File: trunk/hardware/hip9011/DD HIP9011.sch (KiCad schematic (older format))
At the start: 25 parts, among them P1 KNOCK 1, P2 KNOCK 2, P3 12V, P4 CONN_4X2, U1 78L05, X1 4MHz

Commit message: v 2
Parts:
- removed U1: 78L05, TSOP89, symbol 78L05
- removed X1: 4MHz, ~, symbol QUARTZCMS4
- added R10, R11, R12, R13, R14: 1K, ~, symbol R
- added U1: 7805-SOT89, ~, symbol 7805-SOT89
- added X1: QUARTZ, ~, symbol QUARTZ
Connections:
- net labels added: +12V, +5V, CS, GND, INT/HLD, INTOUT, SCK, SI, SO, TEST
- wire segments 78 -> 67
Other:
- note added: "DD HIP9011 ver.2\nRusEfi.com"
- moved on the sheet: C1, C2, C3, C4, C5, C6, C7, C8, D1, D2, P1, P2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

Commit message: with logo
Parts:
- added G1: LOGO, symbol LOGO
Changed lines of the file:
@@
 LIBS:quartz
 LIBS:7805-sot89
+LIBS:logo_flipped
 LIBS:DD HIP9011-cache
 EELAYER 27 0
@@
 Text Notes 1600 1700 0    118  ~ 0
 DD HIP9011 ver.2\nRusEfi.com
+$Comp
+L LOGO G1
+U 1 1 52A2A9AB
+P 2800 5300
+F 0 "G1" H 2800 5197 60  0001 C CNN
+F 1 "LOGO" H 2800 5403 60  0001 C CNN
+F 2 "" H 2800 5300 60  0000 C CNN
+F 3 "" H 2800 5300 60  0000 C CNN
+	1    2800 5300
+	1    0    0    -1
+$EndComp
 $EndSCHEMATC

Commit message: newer version
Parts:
- added R15, R16: 10k, ~, symbol R
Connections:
- net labels added: OUT
- wire segments 67 -> 66
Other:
- note added: "DD HIP9011 ver 0.1\nRusEfi.com"
- note removed: "DD HIP9011 ver.2\nRusEfi.com"
- moved on the sheet: U1
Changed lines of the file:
@@
 Sheet 1 1
 Title "noname.sch"
-Date "7 dec 2013"
+Date "8 dec 2013"
 Rev ""
 Comp ""
@@
 Wire Wire Line
 	2050 4450 2050 4250
-Wire Wire Line
-	2650 4450 2650 4350
 Connection ~ 2200 4450
 Connection ~ 3300 4050
-Connection ~ 2650 4450
 Connection ~ 3300 4450
 Wire Wire Line
@@
 Text Label 7200 4750 0    60   ~ 0
 CS
-Text Label 8500 4750 0    60   ~ 0
-INTOUT
 Wire Wire Line
 	4650 4350 4350 4350
@@
 L 7805-SOT89 U1
 U 1 1 52A25C32
-P 2650 4100
-F 0 "U1" H 2800 3904 60  0000 C CNN
-F 1 "7805-SOT89" H 2650 4300 60  0000 C CNN
-F 2 "~" H 2650 4100 60  0000 C CNN
-F 3 "~" H 2650 4100 60  0000 C CNN
-	1    2650 4100
-	1    0    0    -1
+P 2650 4000
+F 0 "U1" H 2800 3804 60  0000 C CNN
+F 1 "7805-SOT89" H 2650 4200 60  0000 C CNN
+F 2 "~" H 2650 4000 60  0000 C CNN
+F 3 "~" H 2650 4000 60  0000 C CNN
+	1    2650 4000
+	-1   0    0    1
 $EndComp
 Text Label 2200 4050 0    60   ~ 0
 +12V
 Text Notes 1600 1700 0    118  ~ 0
-DD HIP9011 ver.2\nRusEfi.com
+DD HIP9011 ver 0.1\nRusEfi.com
+$Comp
+L R R15
+U 1 1 52A2E159
+P 8400 3450
+F 0 "R15" V 8480 3450 40  0000 C CNN
+F 1 "10k" V 8407 3451 40  0000 C CNN
+F 2 "~" V 8330 3450 30  0000 C CNN
+F 3 "~" H 8400 3450 30  0000 C CNN
+	1    8400 3450
+	1    0    0    -1
+$EndComp
+$Comp
+L R R16
+U 1 1 52A2E168
+P 8400 3950
+F 0 "R16" V 8480 3950 40  0000 C CNN
+F 1 "10k" V 8407 3951 40  0000 C CNN
+F 2 "~" V 8330 3950 30  0000 C CNN
+F 3 "~" H 8400 3950 30  0000 C CNN
+	1    8400 3950
+	1    0    0    -1
+$EndComp
+Text Label 8400 4200 0    60   ~ 0
+GND
+Text Label 8400 3700 0    60   ~ 0
+OUT
+Text Label 8400 3200 0    60   ~ 0
+INTOUT
+Text Label 8500 4750 0    60   ~ 0
+OUT
+Text Label 2650 3750 0    60   ~ 0
+GND
 $Comp
 L LOGO G1
-U 1 1 52A2A9AB
-P 2800 5300
-F 0 "G1" H 2800 5197 60  0001 C CNN
-F 1 "LOGO" H 2800 5403 60  0001 C CNN
-F 2 "" H 2800 5300 60  0000 C CNN
-F 3 "" H 2800 5300 60  0000 C CNN
-	1    2800 5300
-	1    0    0    -1
-$EndComp
+U 1 1 52A3E360
+P 3800 1700
+F 0 "G1" H 3800 1597 60  0001 C CNN
+F 1 "LOGO" H 3800 1803 60  0001 C CNN
+F 2 "" H 3800 1700 60  0000 C CNN
+F 3 "" H 3800 1700 60  0000 C CNN
+	1    3800 1700
+	1    0    0    -1
+$EndComp

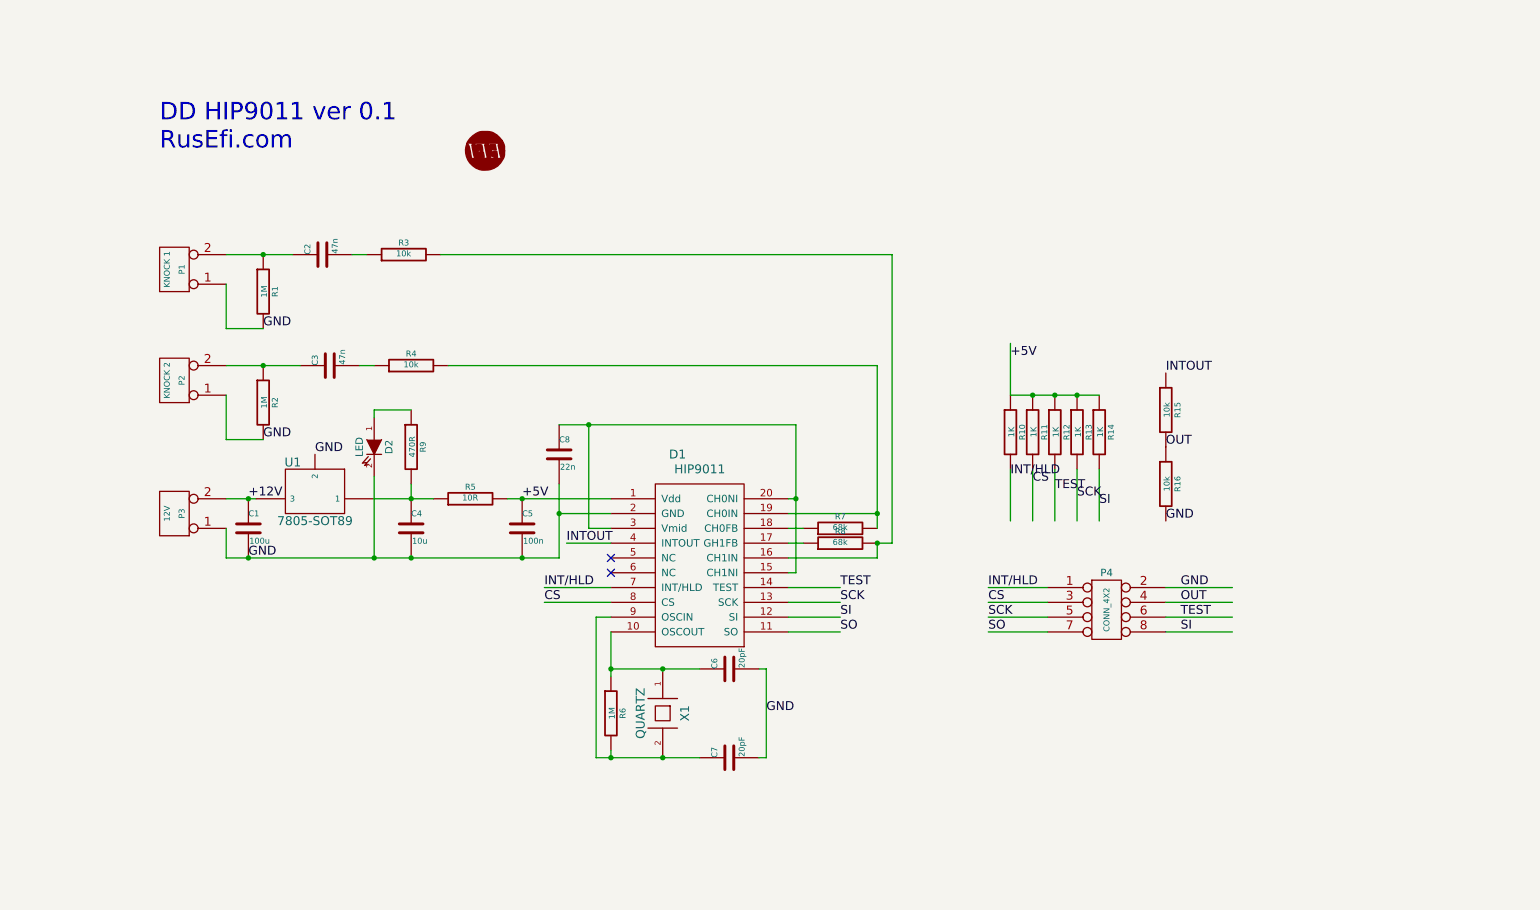
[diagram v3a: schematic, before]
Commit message: 
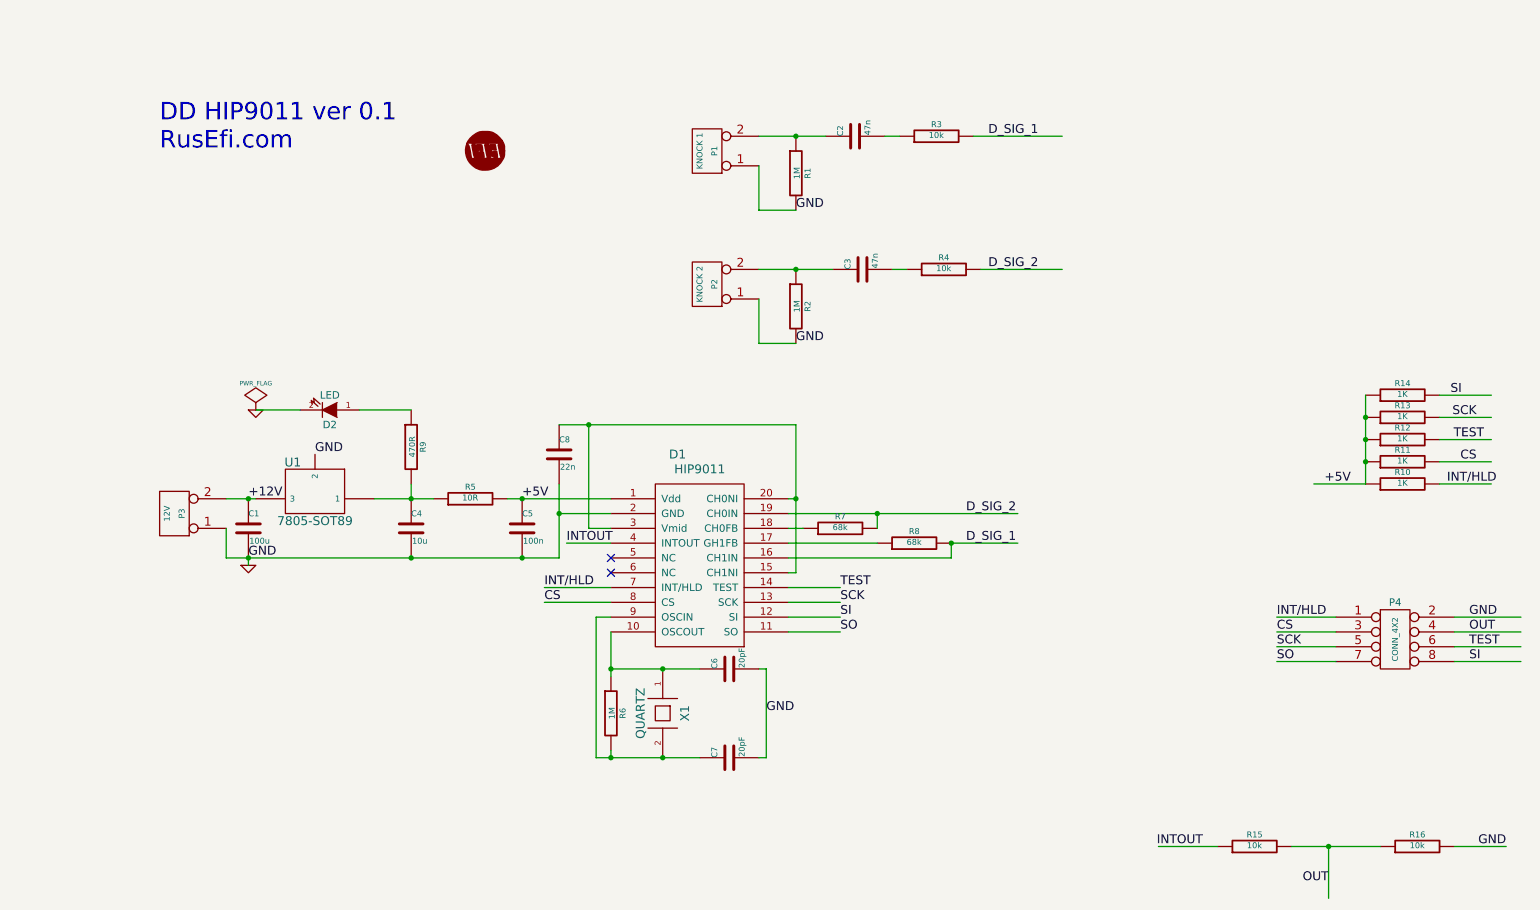
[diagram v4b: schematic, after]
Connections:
- net labels added: D_SIG_1, D_SIG_2
- wire segments 66 -> 69
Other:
- moved on the sheet: C2, C3, D2, P1, P2, P4, R1, R10, R11, R12, R13, R14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

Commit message: 
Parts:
- added D3: DIODE, ~, symbol DIODE
- added D4, D5: ZENER, ~, symbol ZENER
- added Q1: MOS_PRO, symbol MOS_PRO
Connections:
- net labels added: BAT
- wire segments 69 -> 77
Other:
- note added: "Q1 and D3 = reverse polarity protection"
- moved on the sheet: C4, D2, P3, R5, R9, U1

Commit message: 
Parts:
- removed D4, D5: ZENER, ~, symbol ZENER
- removed Q1: MOS_PRO, symbol MOS_PRO
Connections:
- net labels added: +BAT
- net labels removed: BAT
- wire segments 77 -> 70
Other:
- note removed: "Q1 and D3 = reverse polarity protection"
- moved on the sheet: C4, D2, P3, R5, R9, U1

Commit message: proper chip module
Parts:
- removed D3: DIODE, ~, symbol DIODE
- removed G1: LOGO, symbol LOGO
- removed P4: CONN_4X2, symbol CONN_4X2
- added P4: CONN_5X2, symbol CONN_5X2
- added P5, P6: CONN_2, symbol CONN_2
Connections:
- net labels removed: +BAT, D_SIG_1, D_SIG_2
- wire segments 70 -> 63
- no-connect marks 2 -> 7
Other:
- note added: "DD HIP9011 ver.2\nRusEfi.com"
- note removed: "DD HIP9011 ver 0.1\nRusEfi.com"
- moved on the sheet: C2, C3, D2, P1, P2, P3, R1, R10, R11, R12, R13, R14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
